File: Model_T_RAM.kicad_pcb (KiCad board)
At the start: 2 copper layers, 19.8 x 34.3 mm, 4 parts, among them J1 KC-85_RAM, U1 6264, U2 74HC08

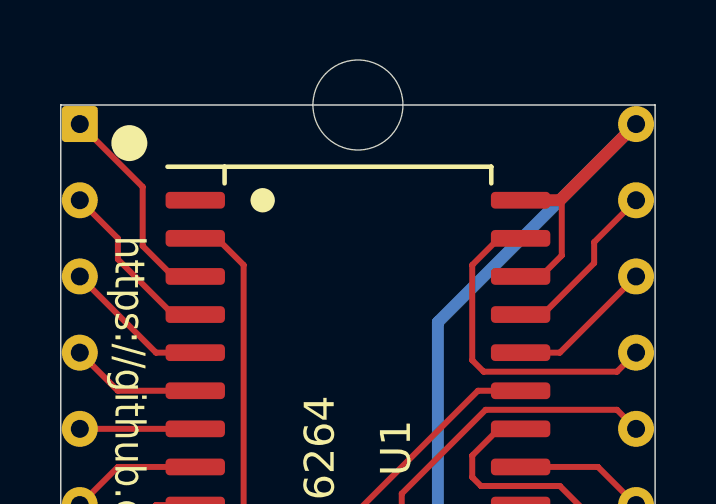
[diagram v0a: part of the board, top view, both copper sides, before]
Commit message: prettify schematic, note power problem, mothball
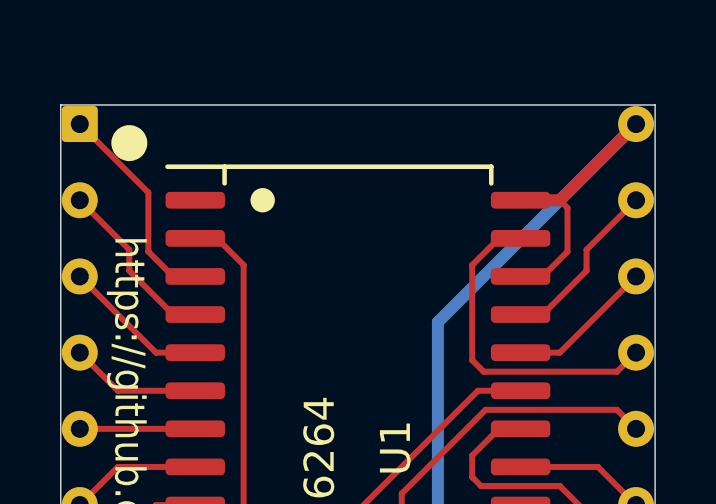
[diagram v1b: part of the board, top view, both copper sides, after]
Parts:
- removed REF**: NPTH_3mm, 000_LOCAL:NPTH_3mm
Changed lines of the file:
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@@
-(kicad_pcb (version 20171130) (host pcbnew 5.1.9-73d0e3b20d~88~ubuntu20.10.1)
+(kicad_pcb (version 20171130) (host pcbnew 5.1.10-88a1d61d58~88~ubuntu20.10.1)
   (general
     (thickness 1.6)
@@
     (tracks 151)
     (zones 0)
-    (modules 4)
+    (modules 3)
     (nets 32)
   )
@@
     (add_net /~WE)
     (add_net GND)
+    (add_net "Net-(U1-Pad1)")
     (add_net "Net-(U2-Pad11)")
     (add_net VCC)
@@
     )
   )
-  (module 000_LOCAL:NPTH_3mm (layer F.Cu)
-    (at 142.24 81.915)
-    (fp_text reference REF** (at 0 2 unlocked) (layer F.SilkS) hide
-      (effects (font (size 1 1) (thickness 0.1)))
-    )
-    (fp_text value NPTH_3mm (at 0 -2) (layer F.Fab)
-      (effects (font (size 1 1) (thickness 0.1)))
-    )
-    (pad "" np_thru_hole circle (at 0 0) (size 3 3) (drill 3) (layers *.Cu *.Mask))
-  )
   (module 000_LOCAL:DIP28_0.73_pcb_sil_pins (layer F.Cu)
     (at 142.24 99.06)
@@
   (segment (start 144.9055 105.41) (end 144.9055 89.1555) (width 0.4) (layer B.Cu) (net 6))
   (via (at 144.9055 105.41) (size 0.5) (drill 0.3) (layers F.Cu B.Cu) (net 6))
-  (segment (start 149.0345 86.9315) (end 149.0345 85.1535) (width 0.2) (layer F.Cu) (net 6))
-  (segment (start 148.336 87.63) (end 149.0345 86.9315) (width 0.2) (layer F.Cu) (net 6))
-  (segment (start 149.0345 85.1535) (end 148.971 85.09) (width 0.2) (layer F.Cu) (net 6))
-  (segment (start 147.6629 87.63) (end 148.336 87.63) (width 0.2) (layer F.Cu) (net 6))
+  (segment (start 149.225 85.344) (end 148.971 85.09) (width 0.2) (layer F.Cu) (net 6))
+  (segment (start 149.225 86.8045) (end 149.225 85.344) (width 0.2) (layer F.Cu) (net 6))
+  (segment (start 148.3995 87.63) (end 149.225 86.8045) (width 0.2) (layer F.Cu) (net 6))
+  (segment (start 147.6629 87.63) (end 148.3995 87.63) (width 0.2) (layer F.Cu) (net 6))
   (segment (start 142.24 95.4405) (end 146.2405 91.44) (width 0.2) (layer F.Cu) (net 7))
   (segment (start 140.5255 106.045) (end 142.24 104.3305) (width 0.2) (layer F.Cu) (net 7))
@@
   (segment (start 137.16 106.68) (end 137.16 110.998) (width 0.2) (layer F.Cu) (net 8))
   (segment (start 138.43 105.41) (end 137.16 106.68) (width 0.2) (layer F.Cu) (net 8))
-  (segment (start 135.0645 86.614) (end 135.0645 84.6455) (width 0.2) (layer F.Cu) (net 9))
-  (segment (start 136.0805 87.63) (end 135.0645 86.614) (width 0.2) (layer F.Cu) (net 9))
-  (segment (start 135.0645 84.6455) (end 132.969 82.55) (width 0.2) (layer F.Cu) (net 9))
+  (segment (start 135.255 84.836) (end 132.969 82.55) (width 0.2) (layer F.Cu) (net 9))
+  (segment (start 135.255 86.8045) (end 135.255 84.836) (width 0.2) (layer F.Cu) (net 9))
+  (segment (start 136.0805 87.63) (end 135.255 86.8045) (width 0.2) (layer F.Cu) (net 9))
   (segment (start 136.8171 87.63) (end 136.0805 87.63) (width 0.2) (layer F.Cu) (net 9))
-  (segment (start 134.239 86.36) (end 132.969 85.09) (width 0.2) (layer F.Cu) (net 10))
-  (segment (start 134.239 87.0585) (end 134.239 86.36) (width 0.2) (layer F.Cu) (net 10))
-  (segment (start 136.0805 88.9) (end 134.239 87.0585) (width 0.2) (layer F.Cu) (net 10))
+  (segment (start 134.62 87.4395) (end 134.62 86.741) (width 0.2) (layer F.Cu) (net 10))
+  (segment (start 134.62 86.741) (end 132.969 85.09) (width 0.2) (layer F.Cu) (net 10))
+  (segment (start 136.0805 88.9) (end 134.62 87.4395) (width 0.2) (layer F.Cu) (net 10))
   (segment (start 136.8171 88.9) (end 136.0805 88.9) (width 0.2) (layer F.Cu) (net 10))
   (segment (start 136.8171 90.17) (end 135.509 90.17) (width 0.2) (layer F.Cu) (net 11))
@@
   (segment (start 151.511 87.63) (end 148.971 90.17) (width 0.2) (layer F.Cu) (net 28))
   (segment (start 148.3995 88.9) (end 147.6629 88.9) (width 0.2) (layer F.Cu) (net 29))
-  (segment (start 150.114 87.1855) (end 148.3995 88.9) (width 0.2) (layer F.Cu) (net 29))
-  (segment (start 150.114 86.487) (end 150.114 87.1855) (width 0.2) (layer F.Cu) (net 29))
-  (segment (start 151.511 85.09) (end 150.114 86.487) (width 0.2) (layer F.Cu) (net 29))
+  (segment (start 149.86 87.4395) (end 148.3995 88.9) (width 0.2) (layer F.Cu) (net 29))
+  (segment (start 149.86 86.741) (end 149.86 87.4395) (width 0.2) (layer F.Cu) (net 29))
+  (segment (start 151.511 85.09) (end 149.86 86.741) (width 0.2) (layer F.Cu) (net 29))
   (segment (start 142.5575 107.315) (end 141.9225 107.95) (width 0.2) (layer F.Cu) (net 30))
   (segment (start 145.923 107.315) (end 142.5575 107.315) (width 0.2) (layer F.Cu) (net 30))

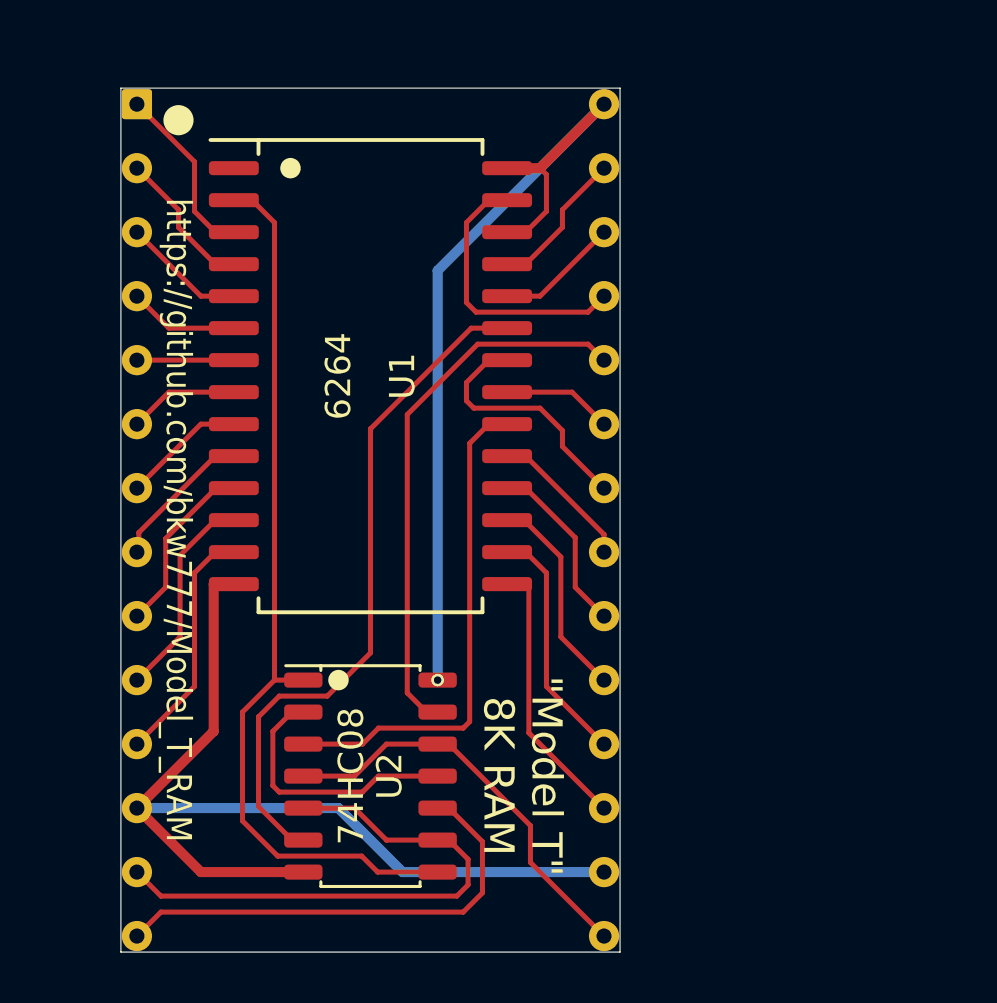
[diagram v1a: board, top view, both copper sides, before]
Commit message: switch to 74HC86 to sleep on standby
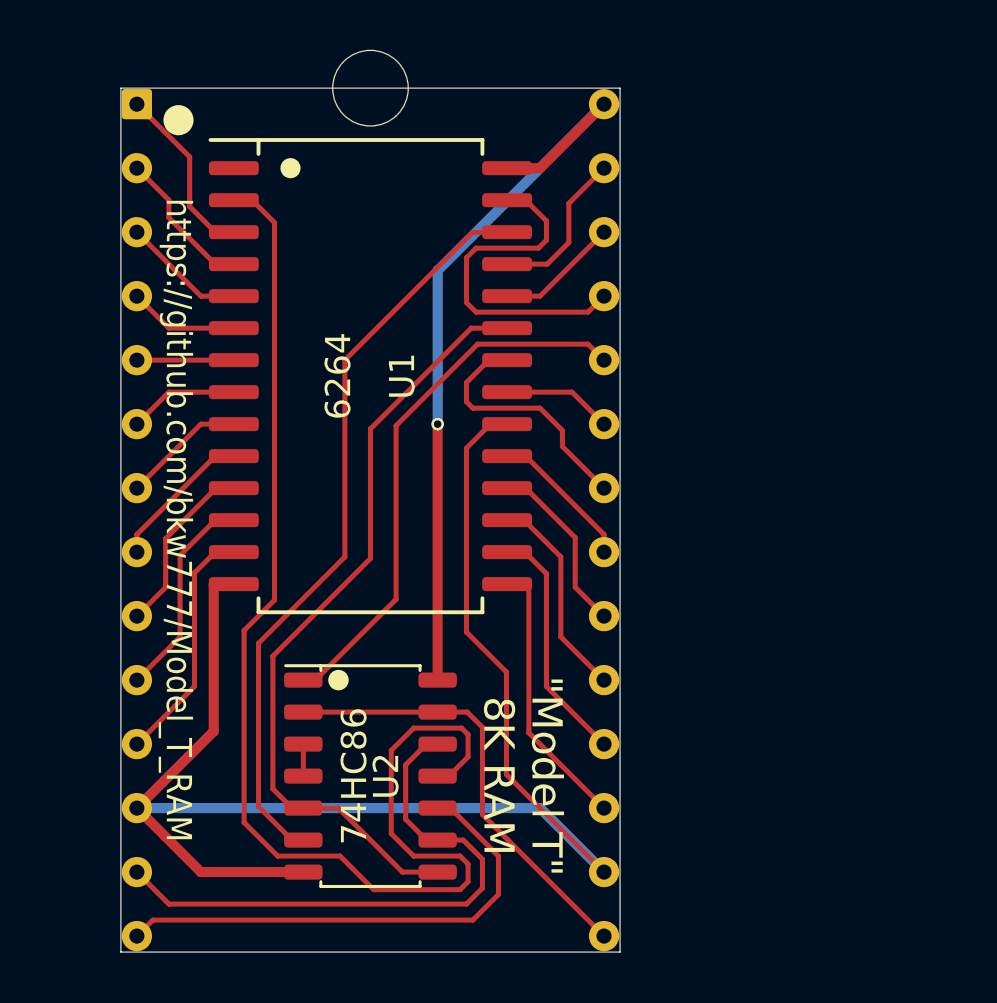
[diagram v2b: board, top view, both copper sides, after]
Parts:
- added REF**: NPTH_3mm, 000_LOCAL:NPTH_3mm, F.Cu at (142.2, 81.9)
- U2: value 74HC08 -> 74HC86; footprint 000_LOCAL:SOIC-14_4x9 -> 000_LOCAL:SOIC-14_3.9x8.7mm_P1.27mm
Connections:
- U1 pad 20: /~CE -> GND
- U1 pad 26: VCC -> /CE2
- U2 pad 1: /A12 -> /~CS_D
- U2 pad 11: Net-(U2-Pad11) -> /A12
- U2 pad 12: /~CS_C -> /~CS_A
- U2 pad 13: /~CS_D -> /~CS_C
- U2 pad 2: Net-(U2-Pad11) -> /~CS_C
- U2 pad 3: /~CE -> Net-(U2-Pad3)
- U2 pad 4: /~CS_C -> Net-(U2-Pad3)
- U2 pad 5: /~CS_A -> /A11
- U2 pad 6: /A11 -> /CE2
- U2 pad 8: /A12 -> /A11
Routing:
- net /CE2: track 0.00 -> 30.0 mm
- net GND: track 38.2 -> 59.3 mm
- net /~CE: track 19.8 -> 0.00 mm
- net /A12: track 36.0 -> 49.9 mm
- net Net-(U2-Pad11): track 10.6 -> 0.00 mm
- net VCC: track 34.2 -> 30.5 mm
- net /A11: track 27.4 -> 30.9 mm
- net /~WE: track 11.0 -> 13.8 mm
- net Net-(U2-Pad3): track 0.00 -> 1.27 mm
- net /~CS_C: track 16.5 -> 17.6 mm
- net /~CS_A: track 22.1 -> 23.1 mm
- net /~CS_B: track 18.8 -> 19.8 mm
- net /A8: track 5.84 -> 6.34 mm
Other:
- board text added: "v004"
- board text removed: "v003"

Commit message: rotate 7486
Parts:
- U2: footprint 000_LOCAL:SOIC-14_3.9x8.7mm_P1.27mm -> 000_LOCAL:SOIC-14_4x9
- moved U1 5.24 mm to (147.3, 94.6)
- moved U2 5.12 mm to (147.3, 109.9), turned to 270 degrees
- moved J1 5.08 mm to (147.3, 99.1)
- moved REF** 5.08 mm to (147.3, 81.9)
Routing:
- net /~CS_B: track 19.8 -> 9.86 mm
- net /~CS_A: track 23.1 -> 14.0 mm
- net /A12: track 49.9 -> 42.0 mm
- net /CE2: track 30.0 -> 22.5 mm
- net GND: track 59.3 -> 52.1 mm
- net VCC: track 30.5 -> 37.3 mm
- net /A11: track 30.9 -> 24.6 mm
- net /~CS_C: track 17.6 -> 13.9 mm
- net /~CS_D: track 21.8 -> 19.9 mm
- net /AD6: track 7.11 -> 5.81 mm
- net /AD2: track 9.65 -> 8.38 mm
- net /AD1: track 8.38 -> 7.11 mm
- net /AD3: track 11.0 -> 9.72 mm
- net /A7: track 7.11 -> 8.38 mm
- net /A6: track 5.84 -> 7.11 mm
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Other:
- board text added: ""Model T" 8K RAM"
- board text added: "github.com/bkw777/Model_T_RAM"
- board text added: "v004 alt"
- board text removed: ""Model T""
- board text removed: "8K RAM"
- board text removed: "https://github.com/bkw777/Model_T_RAM"
- board text removed: "v004"

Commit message: RAM_RST on /CE instead of /OE
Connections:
- J1 pad 22: /~OE -> /RAM_RST
- U1 pad 20: GND -> /RAM_RST
- U1 pad 22: /~OE -> GND
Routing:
- net /~OE: track 9.02 -> 0.00 mm
- net /RAM_RST: track 0.00 -> 4.37 mm
- net GND: track 52.1 -> 54.6 mm
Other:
- board text added: "v005"
- board text removed: "v004 alt"

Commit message: decoupling and ground pour
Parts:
- added C1: 0.1u, 000_LOCAL:C_0805, F.Cu at (153.0, 111.8)
- added C2: 0.1u, 000_LOCAL:C_0805, F.Cu at (152.4, 83.8)
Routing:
- net GND: track 54.6 -> 0.00 mm, vias 0 -> 5
- net VCC: track 37.3 -> 40.5 mm
- added copper zone on B.Cu, net GND
- added copper zone on F.Cu, net GND
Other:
- board text added: "v006"
- board text removed: "v005"

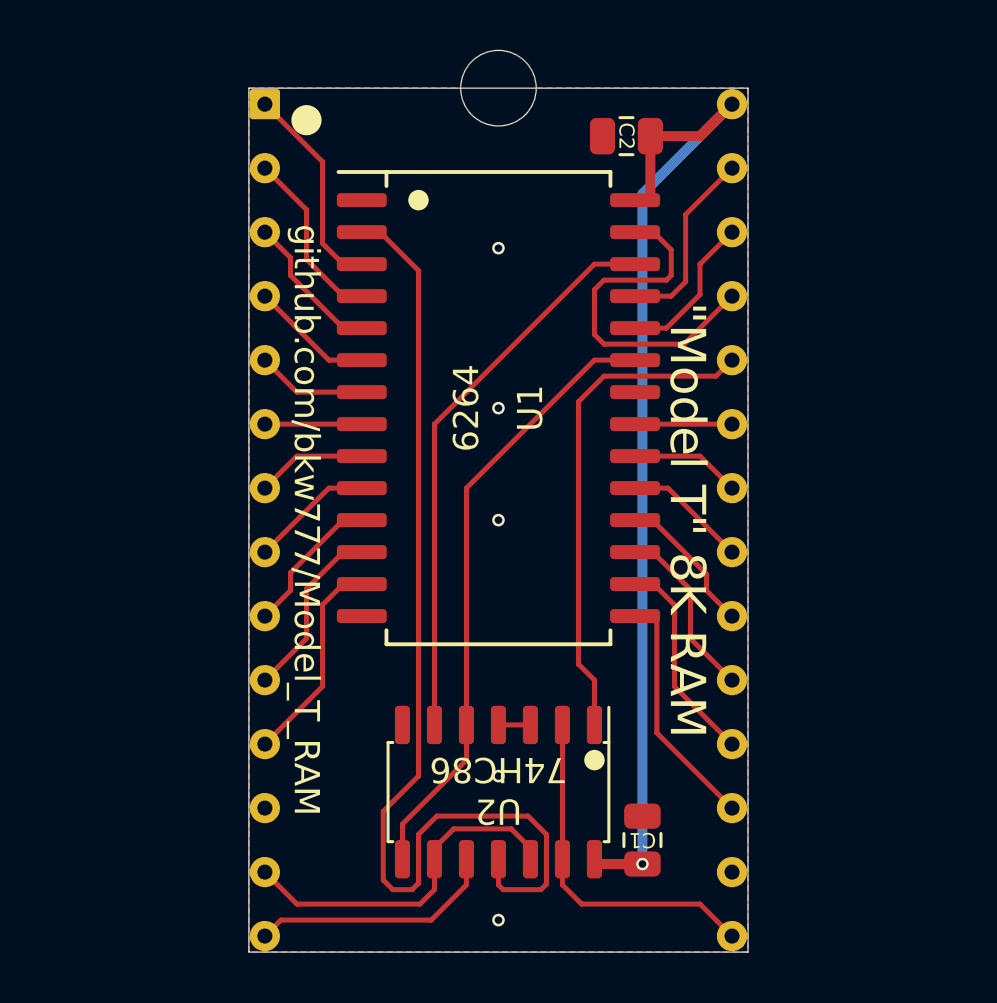
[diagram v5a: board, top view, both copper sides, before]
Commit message: better routing and shielding
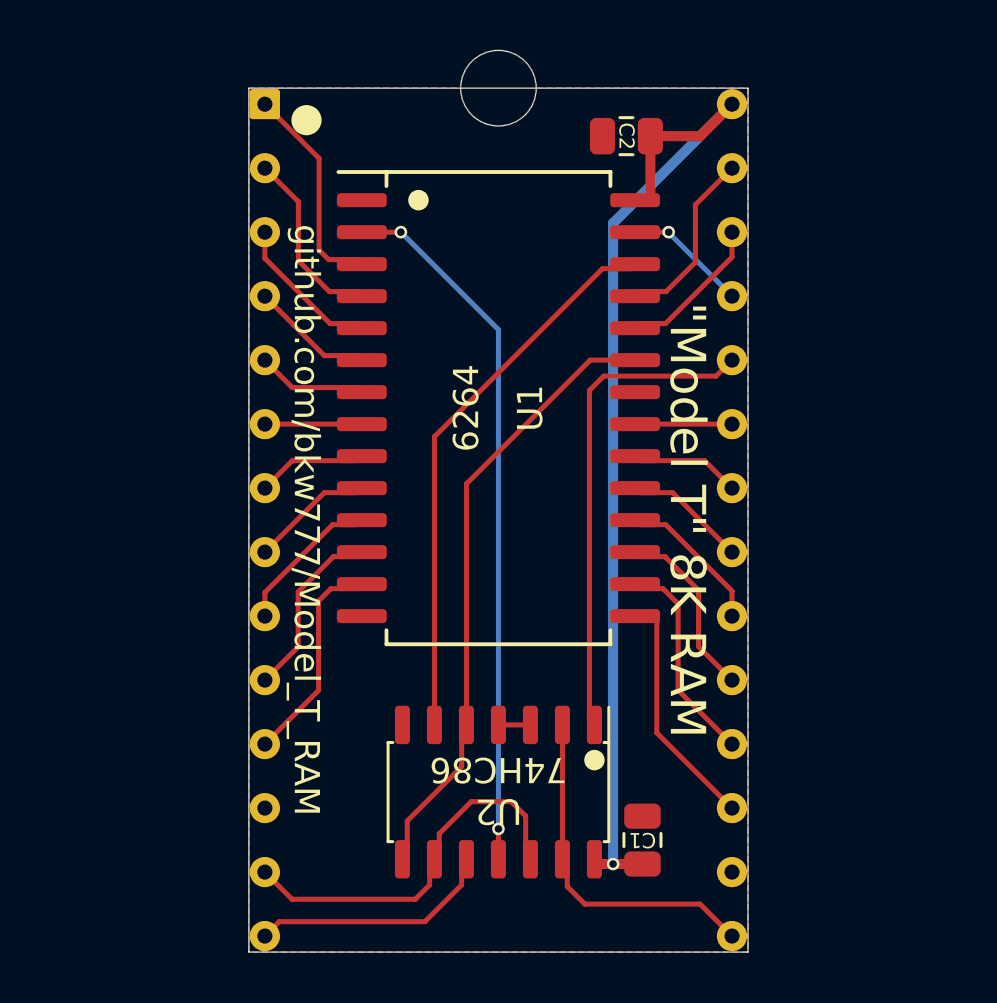
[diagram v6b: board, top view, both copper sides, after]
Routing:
- net /A12: track 42.0 -> 28.0 mm, vias 0 -> 2
- net /~WE: track 14.2 -> 4.92 mm, vias 0 -> 1
- net /~CS_A: track 14.0 -> 15.5 mm
- net GND: vias 5 -> 0
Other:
- board text added: "v007"
- board text removed: "v006"

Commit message: kicad6. 725mil row spacing. pin models.
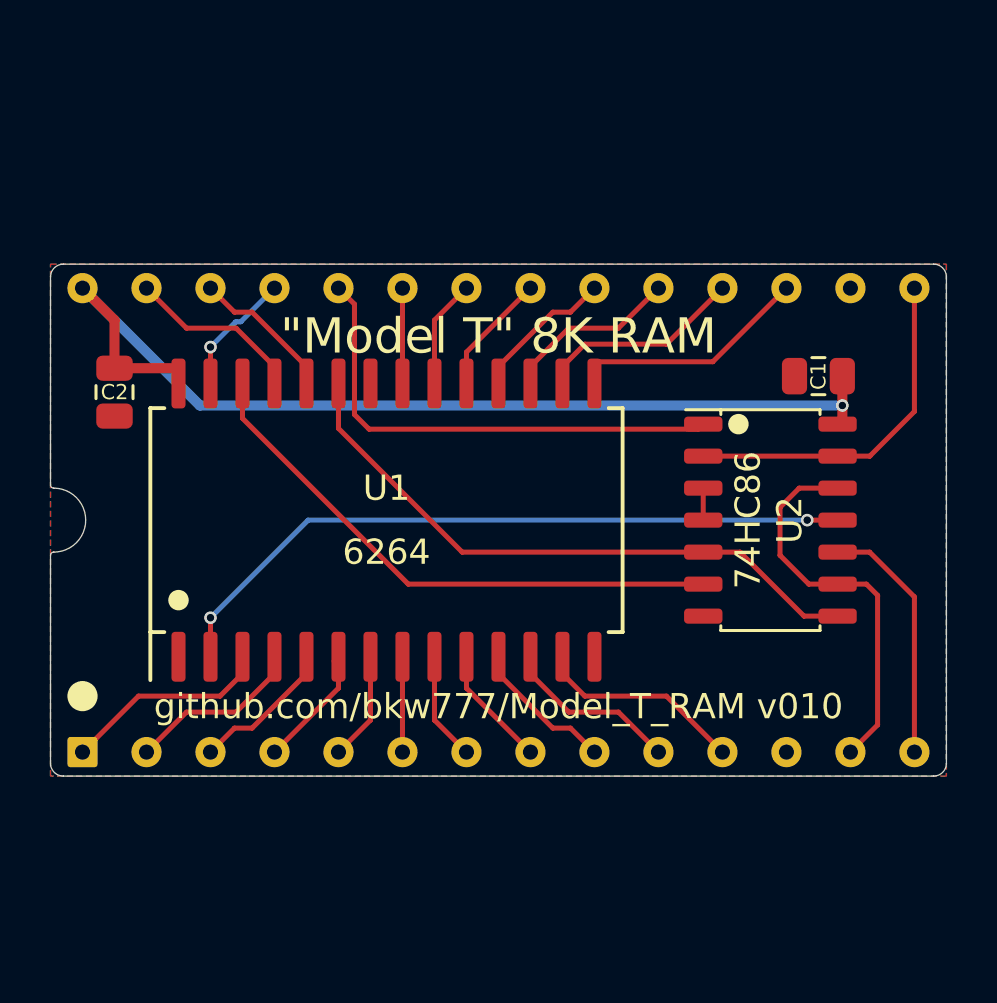
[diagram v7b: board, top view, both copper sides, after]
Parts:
- removed REF**: NPTH_3mm, 000_LOCAL:NPTH_3mm
- J1: footprint 000_LOCAL:DIP28_0.73_pcb_sil_pins -> 000_LOCAL:DIP28_725mils_pcb_pins
- moved C2 22.7 mm to (132.1, 94.0), turned to -90 degrees
- moved C1 19.7 mm to (160.0, 93.3), turned to 180 degrees
- moved U2 15.3 mm to (158.1, 99.1), turned to 0 degrees
- moved U1 6.29 mm to (142.9, 99.1), turned to 90 degrees
- turned J1 to 90 degrees
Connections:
- net /~CS_A renamed /~{CS_A}
- net /~CS_B renamed /~{CS_B}
- net /~CS_C renamed /~{CS_C}
- net /~CS_D renamed /~{CS_D}
- net /~WE renamed /~{WE}
- U1 pad 1: (no net) -> unconnected-(U1-Pad1)
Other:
- board size 19.8 x 34.3 mm -> 35.6 x 20.3 mm
- net class Default removed
- board text added: "${COMMENT1} v${REVISION}"
- board text added: "Kyotronic KC-85 TRS-80 Model 100 NEC PC-8201 / PC-8300 Olivetti M10"
- board text added: "Row spacing is 725mils, not 700, not an error."
- board text removed: "Kyotronic KC-85"
- board text removed: "NEC PC-8201 / PC-8201A"
- board text removed: "Olivetti M10"
- board text removed: "TRS-80 Model 100"
- board text removed: "github.com/bkw777/Model_T_RAM"
- board text removed: "v007"

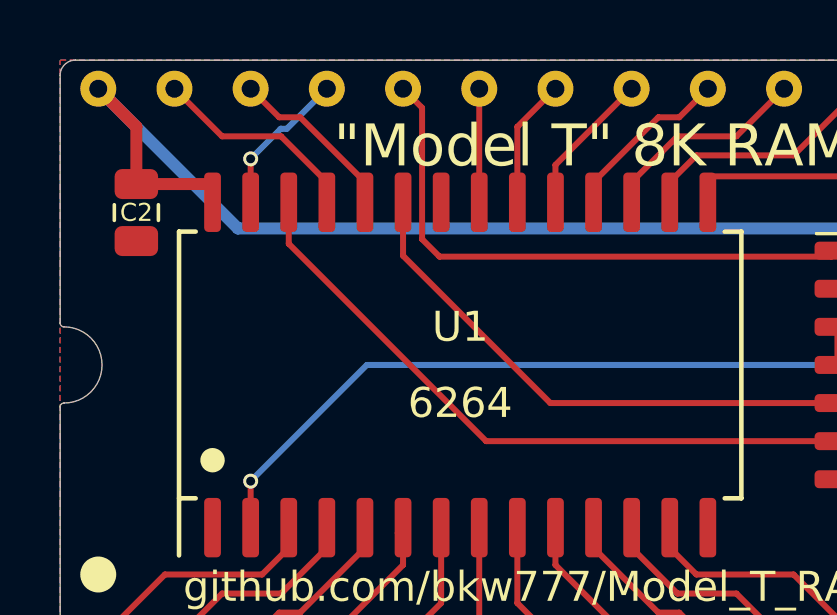
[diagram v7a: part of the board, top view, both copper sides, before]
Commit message: add type b variant
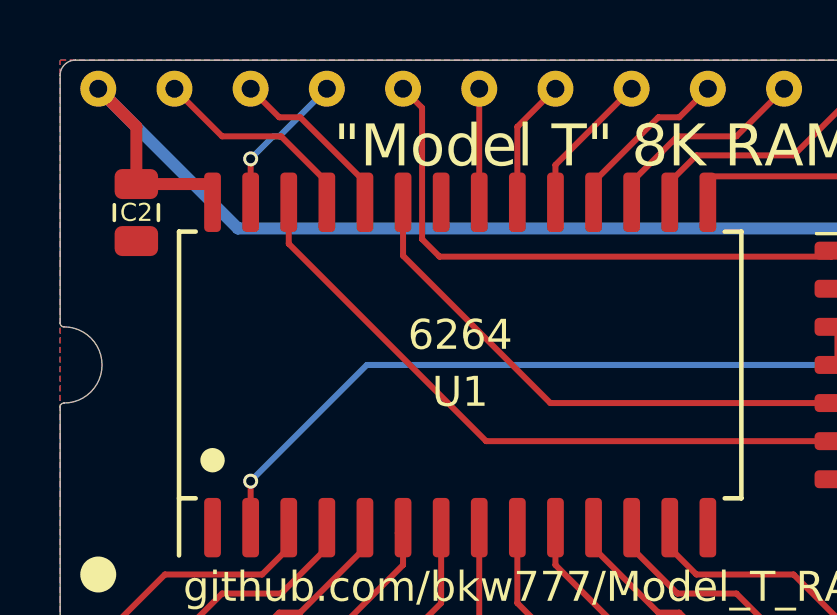
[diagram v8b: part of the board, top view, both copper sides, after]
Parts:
- U1: footprint 000_LOCAL:AS6C6264-55SCN -> 000_LOCAL:SSOP-28
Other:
- board text removed: "Row spacing is 725mils, not 700, not an error."
